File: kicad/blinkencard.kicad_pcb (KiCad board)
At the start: 4 copper layers, 88.9 x 50.8 mm, 64 parts, among them Q1 BC847, Q2 BC847, Q3 BC847, Q4 BC847, Q5 BC847, U1 ICE40UP5K-SG48ITR, U2 ESP32-WROOM-32D

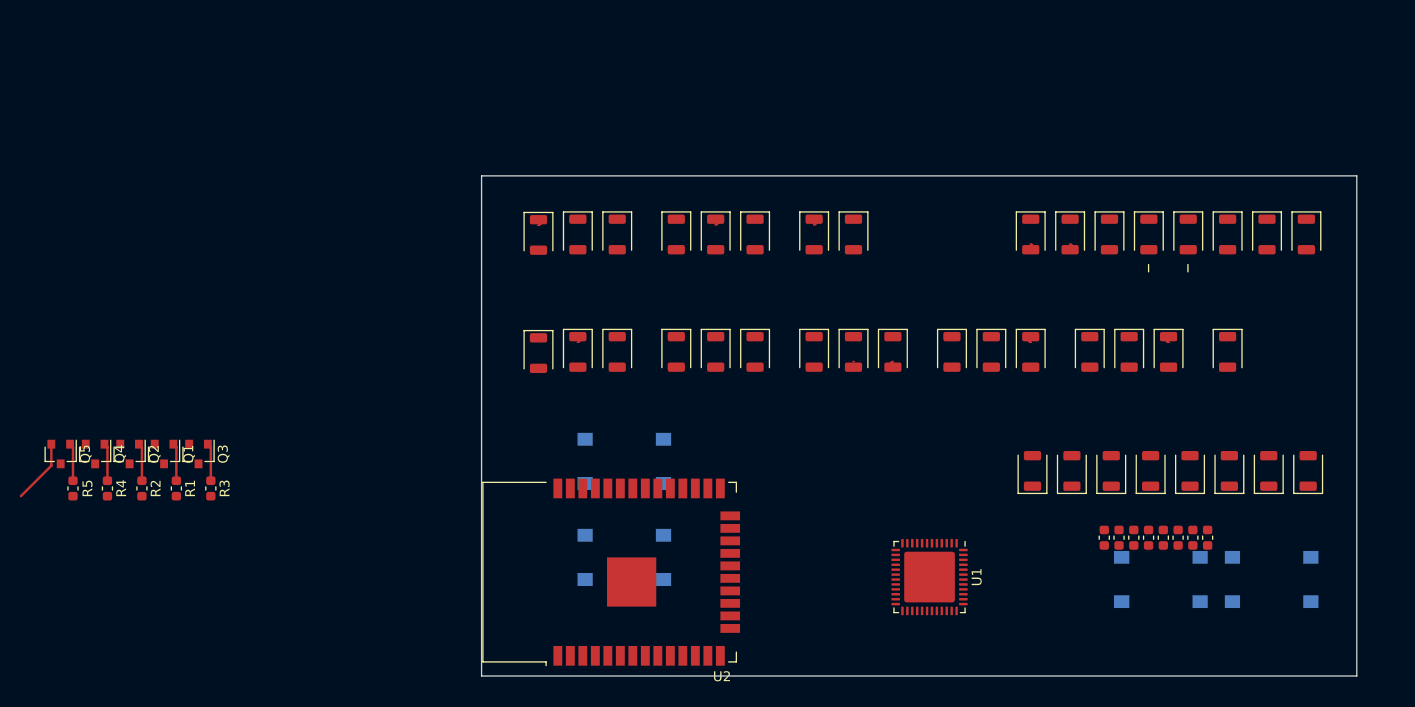
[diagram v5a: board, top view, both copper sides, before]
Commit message: Use CP2102A USB-UART and GPIO instead of ESP32 to keep it simple. Add power section and start routing.
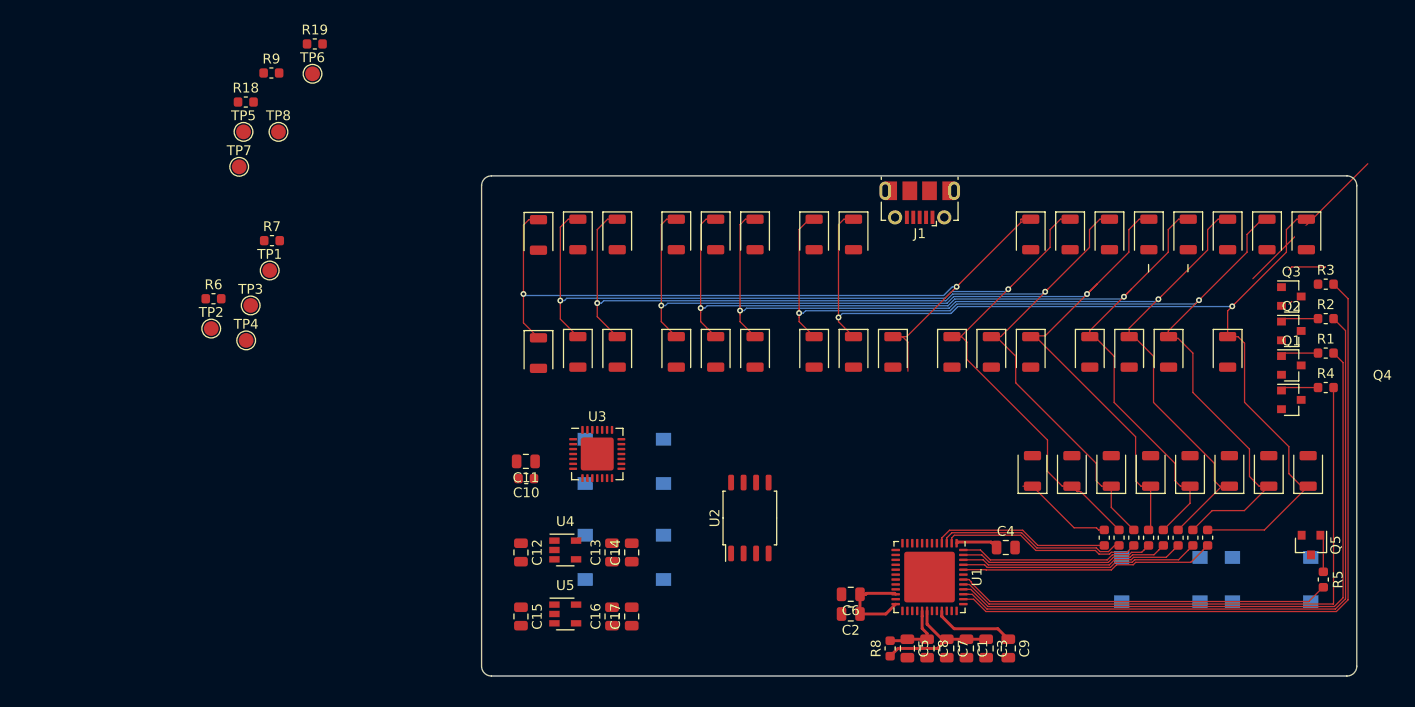
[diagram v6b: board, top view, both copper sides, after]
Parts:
- added C1: 0.01uF, Capacitor_SMD:C_0805_2012Metric, F.Cu at (49.2, 48.0)
- added C10: .1uF, Capacitor_SMD:C_0603_1608Metric, F.Cu at (4.54, 30.8)
- added C11: 4.7uF, Capacitor_SMD:C_0805_2012Metric, F.Cu at (4.50, 29.0)
- added C12: 1.0uF, Capacitor_SMD:C_0805_2012Metric, F.Cu at (4.00, 38.2)
- added C13: 1.0uF, Capacitor_SMD:C_0805_2012Metric, F.Cu at (13.2, 38.2)
- added C14: 10uF, Capacitor_SMD:C_0805_2012Metric, F.Cu at (15.2, 38.2)
- added C15: 1.0uF, Capacitor_SMD:C_0805_2012Metric, F.Cu at (4.00, 44.8)
- added C16: 1.0uF, Capacitor_SMD:C_0805_2012Metric, F.Cu at (13.2, 44.8)
- added C17: 10uF, Capacitor_SMD:C_0805_2012Metric, F.Cu at (15.2, 44.8)
- added C2: 0.01uF, Capacitor_SMD:C_0805_2012Metric, F.Cu at (37.5, 44.5)
- added C3: 0.1uF, Capacitor_SMD:C_0805_2012Metric, F.Cu at (51.2, 48.0)
- added C4: 0.1uF, Capacitor_SMD:C_0805_2012Metric, F.Cu at (53.2, 37.8)
- added C5: 0.01uF, Capacitor_SMD:C_0805_2012Metric, F.Cu at (43.2, 48.0)
- added C6: 0.1uF, Capacitor_SMD:C_0805_2012Metric, F.Cu at (37.5, 42.5)
- added C7: 1uF, Capacitor_SMD:C_0805_2012Metric, F.Cu at (47.2, 48.0)
- added C8: 0.1uF, Capacitor_SMD:C_0805_2012Metric, F.Cu at (45.2, 48.0)
- added C9: 0.1uF, Capacitor_SMD:C_0805_2012Metric, F.Cu at (53.5, 48.0)
- added J1: USB_B_Micro, Connector_USB:USB_Micro-B_Molex-105017-0001, F.Cu at (44.5, 2.75)
- added R18: 47.5K, Resistor_SMD:R_0603_1608Metric, F.Cu at (-23.9, -7.50)
- added R19: 10k, Resistor_SMD:R_0603_1608Metric, F.Cu at (-16.9, -13.4)
- added R6: 10K, Resistor_SMD:R_0603_1608Metric, F.Cu at (-27.2, 12.5)
- added R7: 10K, Resistor_SMD:R_0603_1608Metric, F.Cu at (-21.3, 6.58)
- added R8: 100, Resistor_SMD:R_0603_1608Metric, F.Cu at (41.5, 48.0)
- added R9: 22.1K, Resistor_SMD:R_0603_1608Metric, F.Cu at (-21.4, -10.4)
- added TP1: IOT_49a, TestPoint:TestPoint_Pad_D1.5mm, F.Cu at (-21.5, 9.61)
- added TP2: IOT_48b, TestPoint:TestPoint_Pad_D1.5mm, F.Cu at (-27.5, 15.5)
- added TP3: IOT_46b_G0, TestPoint:TestPoint_Pad_D1.5mm, F.Cu at (-23.4, 13.2)
- added TP4: IOT_45a_G1, TestPoint:TestPoint_Pad_D1.5mm, F.Cu at (-23.9, 16.7)
- added TP5: FPGA_RTS, TestPoint:TestPoint_Pad_D1.5mm, F.Cu at (-24.2, -4.47)
- added TP6: FPGA_CTS, TestPoint:TestPoint_Pad_D1.5mm, F.Cu at (-17.2, -10.4)
- added TP7: FPGA_TXO, TestPoint:TestPoint_Pad_D1.5mm, F.Cu at (-24.6, -0.92)
- added TP8: FPGA_RXI, TestPoint:TestPoint_Pad_D1.5mm, F.Cu at (-20.6, -4.47)
- added U3: CP2102N-A01-GQFN28, Package_DFN_QFN:QFN-28-1EP_5x5mm_P0.5mm_EP3.35x3.35mm, F.Cu at (11.8, 28.2)
- added U4: MIC5504-1.2YM5, Package_TO_SOT_SMD:SOT-23-5, F.Cu at (8.50, 38.0)
- added U5: MIC5504-3.3YM5, Package_TO_SOT_SMD:SOT-23-5, F.Cu at (8.50, 44.5)
- SW1: renamed from REF**; value SW_SPST_PTS645 -> 0
- SW2: renamed from REF**; value SW_SPST_PTS645 -> 1
- SW3: renamed from REF**; value SW_SPST_PTS645 -> LEFT
- SW4: renamed from REF**; value SW_SPST_PTS645 -> RIGHT
- U2: value ESP32-WROOM-32D -> W25Q64JV; footprint RF_Module:ESP32-WROOM-32 -> Package_SO:SOIC-8_5.23x5.23mm_P1.27mm
- moved Q5 127.3 mm to (84.2, 37.5)
- moved R5 127.3 mm to (85.5, 41.0)
- moved R4 124.2 mm to (85.8, 21.5), turned to 0 degrees
- moved Q4 121.6 mm to (82.2, 22.8), turned to 0 degrees
- moved R2 121.5 mm to (85.8, 14.5), turned to 0 degrees
- moved Q2 118.7 mm to (82.2, 15.8), turned to 0 degrees
- moved R1 117.6 mm to (85.8, 18.0), turned to 0 degrees
- moved R3 115.1 mm to (85.8, 11.0), turned to 0 degrees
- moved Q1 114.9 mm to (82.2, 19.2), turned to 0 degrees
- moved Q3 112.1 mm to (82.2, 12.2), turned to 0 degrees
- moved U2 12.5 mm to (27.2, 34.8)
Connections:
- D10 pad 1: Net-(D17-Pad1) -> Net-(D10-Pad1)
- D10 pad 2: Net-(D20-Pad2) -> Net-(D10-Pad2)
- D11 pad 1: Net-(D16-Pad1) -> Net-(D11-Pad1)
- D11 pad 2: Net-(D20-Pad2) -> Net-(D10-Pad2)
- D12 pad 1: Net-(D15-Pad1) -> Net-(D12-Pad1)
- D12 pad 2: Net-(D20-Pad2) -> Net-(D10-Pad2)
- D13 pad 1: Net-(D14-Pad1) -> Net-(D13-Pad1)
- D13 pad 2: Net-(D20-Pad2) -> Net-(D10-Pad2)
- D14 pad 1: Net-(D13-Pad1) -> Net-(D14-Pad1)
- D14 pad 2: Net-(D20-Pad2) -> Net-(D10-Pad2)
- D15 pad 1: Net-(D12-Pad1) -> Net-(D15-Pad1)
- D15 pad 2: Net-(D20-Pad2) -> Net-(D10-Pad2)
- D16 pad 1: Net-(D11-Pad1) -> Net-(D16-Pad1)
- D16 pad 2: Net-(D20-Pad2) -> Net-(D10-Pad2)
- D17 pad 1: Net-(D10-Pad1) -> Net-(D17-Pad1)
- D17 pad 2: Net-(D20-Pad2) -> Net-(D10-Pad2)
- D20 pad 2: Net-(D10-Pad2) -> Net-(D20-Pad2)
- D21 pad 2: Net-(D10-Pad2) -> Net-(D20-Pad2)
- D22 pad 2: Net-(D10-Pad2) -> Net-(D20-Pad2)
- D23 pad 2: Net-(D10-Pad2) -> Net-(D20-Pad2)
- D24 pad 2: Net-(D10-Pad2) -> Net-(D20-Pad2)
- D25 pad 2: Net-(D10-Pad2) -> Net-(D20-Pad2)
- D26 pad 2: Net-(D10-Pad2) -> Net-(D20-Pad2)
- D27 pad 2: Net-(D10-Pad2) -> Net-(D20-Pad2)
- D30 pad 1: Net-(D17-Pad1) -> Net-(D10-Pad1)
- D30 pad 2: Net-(D40-Pad2) -> Net-(D30-Pad2)
- D31 pad 1: Net-(D16-Pad1) -> Net-(D11-Pad1)
- D31 pad 2: Net-(D40-Pad2) -> Net-(D30-Pad2)
- D32 pad 1: Net-(D15-Pad1) -> Net-(D12-Pad1)
- D32 pad 2: Net-(D40-Pad2) -> Net-(D30-Pad2)
- D33 pad 1: Net-(D14-Pad1) -> Net-(D13-Pad1)
- D33 pad 2: Net-(D40-Pad2) -> Net-(D30-Pad2)
- D34 pad 1: Net-(D13-Pad1) -> Net-(D14-Pad1)
- D34 pad 2: Net-(D40-Pad2) -> Net-(D30-Pad2)
- D35 pad 1: Net-(D12-Pad1) -> Net-(D15-Pad1)
- D35 pad 2: Net-(D40-Pad2) -> Net-(D30-Pad2)
- D36 pad 1: Net-(D11-Pad1) -> Net-(D16-Pad1)
- D36 pad 2: Net-(D40-Pad2) -> Net-(D30-Pad2)
- D37 pad 1: Net-(D10-Pad1) -> Net-(D17-Pad1)
- D37 pad 2: Net-(D40-Pad2) -> Net-(D30-Pad2)
- D40 pad 2: Net-(D30-Pad2) -> Net-(D40-Pad2)
- D41 pad 2: Net-(D30-Pad2) -> Net-(D40-Pad2)
- D42 pad 2: Net-(D30-Pad2) -> Net-(D40-Pad2)
- D43 pad 2: Net-(D30-Pad2) -> Net-(D40-Pad2)
- D44 pad 2: Net-(D30-Pad2) -> Net-(D40-Pad2)
- D45 pad 2: Net-(D30-Pad2) -> Net-(D40-Pad2)
- D46 pad 2: Net-(D30-Pad2) -> Net-(D40-Pad2)
- D47 pad 2: Net-(D30-Pad2) -> Net-(D40-Pad2)
- D50 pad 1: Net-(D17-Pad1) -> Net-(D10-Pad1)
- D51 pad 1: Net-(D16-Pad1) -> Net-(D11-Pad1)
- D52 pad 1: Net-(D15-Pad1) -> Net-(D12-Pad1)
- D53 pad 1: Net-(D14-Pad1) -> Net-(D13-Pad1)
- D54 pad 1: Net-(D13-Pad1) -> Net-(D14-Pad1)
- D55 pad 1: Net-(D12-Pad1) -> Net-(D15-Pad1)
- D56 pad 1: Net-(D11-Pad1) -> Net-(D16-Pad1)
- D57 pad 1: Net-(D10-Pad1) -> Net-(D17-Pad1)
- SW1 pad 1: (no net) -> BUTTON_0
- SW1 pad 2: (no net) -> GND
- SW2 pad 1: (no net) -> BUTTON_1
- SW2 pad 2: (no net) -> GND
- SW3 pad 1: (no net) -> BUTTON_L
- SW3 pad 2: (no net) -> GND
- SW4 pad 1: (no net) -> BUTTON_R
- SW4 pad 2: (no net) -> GND
- U1 pad 10: LED_ROW_2 -> Net-(U1-Pad10)
- U1 pad 11: LED_ROW_1 -> FPGA_RTS
- U1 pad 12: LED_ROW_0 -> FPGA_CTS
- U1 pad 14: Net-(U1-Pad14) -> FPGA_SO_FLASH_MOSI
- U1 pad 15: Net-(U1-Pad15) -> FPGA_SCK
- U1 pad 16: Net-(U1-Pad16) -> FPGA_SS
- U1 pad 17: Net-(U1-Pad17) -> FPGA_SI_FLASH_MISO
- U1 pad 19: Net-(U1-Pad19) -> FLASH_HOLDn
- U1 pad 23: Net-(U1-Pad23) -> BUTTON_1
- U1 pad 25: Net-(U1-Pad25) -> BUTTON_0
- U1 pad 26: Net-(U1-Pad26) -> BUTTON_R
- U1 pad 27: Net-(U1-Pad27) -> BUTTON_L
- U1 pad 29: +1V2 -> Net-(C5-Pad1)
- U1 pad 38: Net-(U1-Pad38) -> LED_ROW_2
- U1 pad 39: Net-(U1-Pad39) -> LED_ROW_1
- U1 pad 40: Net-(U1-Pad40) -> LED_ROW_0
- U1 pad 41: Net-(U1-Pad41) -> LED_ROW_3
- U1 pad 42: Net-(U1-Pad42) -> LED_ROW_4
- U1 pad 6: LED_ROW_4 -> Net-(U1-Pad6)
- U1 pad 7: Net-(U1-Pad7) -> FPGA_CDONE
- U1 pad 8: Net-(U1-Pad8) -> FPGA_CRESET
- U1 pad 9: LED_ROW_3 -> Net-(U1-Pad9)
- U2 pad 1: Net-(U2-Pad1) -> FPGA_SS
- U2 pad 2: Net-(U2-Pad2) -> FPGA_SI_FLASH_MISO
- U2 pad 3: Net-(U2-Pad3) -> VDD
- U2 pad 4: Net-(U2-Pad4) -> GND
- U2 pad 5: Net-(U2-Pad5) -> FPGA_SO_FLASH_MOSI
- U2 pad 6: Net-(U2-Pad6) -> FPGA_SCK
- U2 pad 7: Net-(U2-Pad7) -> FLASH_HOLDn
- U2 pad 8: Net-(U2-Pad8) -> VDD
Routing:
- net Net-(D10-Pad1): track 0.00 -> 108.7 mm, vias 0 -> 2
- net Net-(D12-Pad1): track 0.00 -> 104.7 mm, vias 0 -> 2
- net Net-(D11-Pad1): track 1.57 -> 106.0 mm, vias 0 -> 2
- net Net-(D14-Pad1): track 0.00 -> 101.2 mm, vias 0 -> 2
- net Net-(D15-Pad1): track 0.00 -> 100.7 mm, vias 0 -> 2
- net Net-(D17-Pad1): track 1.57 -> 101.7 mm, vias 0 -> 2
- net Net-(D13-Pad1): track 3.15 -> 102.8 mm, vias 0 -> 2
- net Net-(D16-Pad1): track 2.59 -> 101.3 mm, vias 0 -> 2
- net LED_ROW_2: track 0.00 -> 72.8 mm
- net LED_ROW_1: track 0.00 -> 68.8 mm
- net LED_ROW_0: track 0.00 -> 64.9 mm
- net LED_ROW_3: track 0.00 -> 60.4 mm
- net LED_ROW_4: track 0.00 -> 38.2 mm
- net LED_COL_7: track 0.00 -> 25.9 mm
- net LED_COL_6: track 0.00 -> 24.3 mm
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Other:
- outline, holes or cut-outs redrawn
- copper layers 4 -> 2
- net class Default: clearance 0.2 -> 0.127; trace_width 0.25 -> 0.127; via_dia 0.8 -> 0.6; via_drill 0.4 -> 0.3
- rule pad_to_mask_clearance: 0.051 -> 0.2
- rule trace_clearance: 0.2 -> 0.127
- rule trace_min: 0.2 -> 0.127
- rule via_min_size: 0.4 -> 0.6

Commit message: LED routing
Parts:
- removed the Q4 at (82.2, 22.8)
- added Q1: BC847, Package_TO_SOT_SMD:SOT-23, F.Cu at (82.2, 22.8)
- turned D50 to 270 degrees
- turned D51 to 270 degrees
- turned D52 to 270 degrees
- turned D53 to 270 degrees
- turned D54 to 270 degrees
- turned D55 to 270 degrees
- turned D56 to 270 degrees
- turned D57 to 270 degrees
- renumbered Q1 to Q2, Q2 to Q3, Q3 to Q4, R4 to R1, R1 to R2, R2 to R3, R3 to R4
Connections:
- Q2 pad 2: Net-(D10-Pad2) -> Net-(D20-Pad2)
- Q3 pad 2: Net-(D20-Pad2) -> Net-(D30-Pad2)
- Q4 pad 2: Net-(D30-Pad2) -> Net-(D40-Pad2)
- R1 pad 2: LED_ROW_3 -> LED_ROW_0
- R2 pad 2: LED_ROW_0 -> LED_ROW_1
- R3 pad 2: LED_ROW_1 -> LED_ROW_2
- R4 pad 2: LED_ROW_2 -> LED_ROW_3
- U1 pad 38: LED_ROW_2 -> LED_ROW_3
- U1 pad 39: LED_ROW_1 -> LED_ROW_2
- U1 pad 40: LED_ROW_0 -> LED_ROW_1
- U1 pad 41: LED_ROW_3 -> LED_ROW_0
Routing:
- net Net-(D30-Pad2): track 0.00 -> 92.4 mm, vias 0 -> 9
- net Net-(D10-Pad2): track 0.00 -> 78.3 mm, vias 0 -> 2
- net Net-(D40-Pad2): track 0.00 -> 45.9 mm, vias 0 -> 9
- net Net-(D20-Pad2): track 0.00 -> 43.1 mm, vias 0 -> 9
- net Net-(D50-Pad2): track 0.00 -> 40.0 mm, vias 0 -> 8
- net Net-(D10-Pad1): track 108.7 -> 91.9 mm
- net VDD: track 22.4 -> 38.4 mm, vias 0 -> 4
- net Net-(D12-Pad1): track 104.7 -> 91.8 mm
- net LED_ROW_3: track 60.4 -> 72.8 mm
- net Net-(D11-Pad1): track 106.0 -> 93.7 mm
- net Net-(D13-Pad1): track 102.8 -> 91.5 mm
- net Net-(D14-Pad1): track 101.2 -> 93.7 mm
- net Net-(D16-Pad1): track 101.3 -> 94.2 mm
- net Net-(D15-Pad1): track 100.7 -> 94.1 mm
- net Net-(D17-Pad1): track 101.7 -> 96.7 mm
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
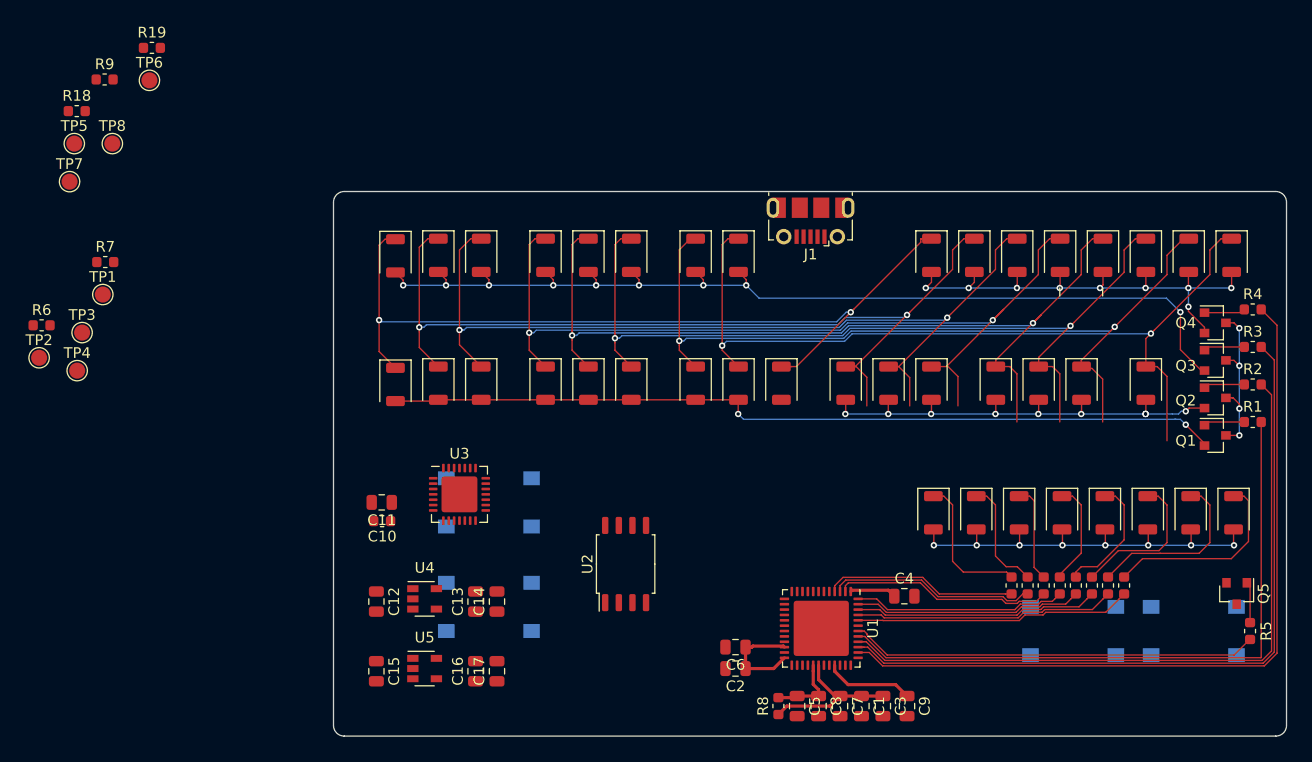
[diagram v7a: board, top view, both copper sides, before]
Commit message: Mostly routed
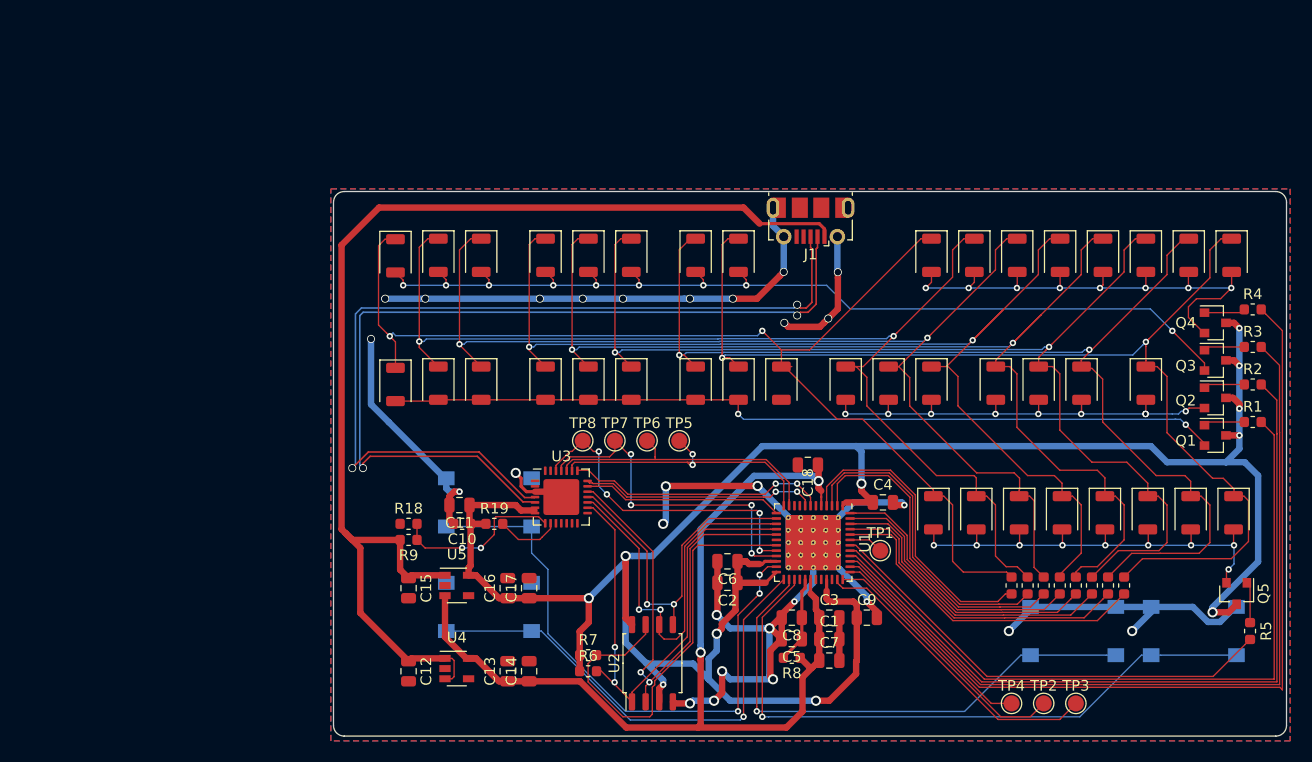
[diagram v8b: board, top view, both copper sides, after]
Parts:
- added C18: 0.1uF, Capacitor_SMD:C_0805_2012Metric, F.Cu at (44.2, 25.5)
- D10, D11, D12, D13, D14, D15, D16, D17, D20, D21, D22, D23, D24, D25, D26, D27, D30, D31, D32, D33, D34, D35, D36, D37, D40, D41, D42, D43, D44, D45, D46, D47, D50, D51, D52, D53, D54, D55, D56, D57: footprint LED_SMD:LED_1206_3216Metric_ReverseMount_Hole1.8x2.4mm -> blinkencard:LED_1206_3216Metric_ReverseMount_Hole1.8x2.4mm
- J1: footprint Connector_USB:USB_Micro-B_Molex-105017-0001 -> blinkencard:USB_Micro-B_Molex-105017-0001
- U1: footprint Package_DFN_QFN:QFN-48-1EP_7x7mm_P0.5mm_EP5.15x5.15mm -> Package_DFN_QFN:QFN-48-1EP_7x7mm_P0.5mm_EP5.15x5.15mm_ThermalVias
- U2: footprint Package_SO:SOIC-8_5.23x5.23mm_P1.27mm -> Package_SO:SOIC-8_5.275x5.275mm_P1.27mm
- moved TP2 99.1 mm to (66.2, 47.8)
- moved TP3 98.9 mm to (69.2, 47.8)
- moved TP4 92.5 mm to (63.2, 47.8)
- moved TP1 76.4 mm to (51.0, 33.5)
- moved TP5 62.9 mm to (32.2, 23.2)
- moved R6 60.3 mm to (23.8, 44.8)
- moved R7 58.1 mm to (23.8, 43.2)
- moved TP6 57.3 mm to (29.2, 23.2)
- moved TP7 56.3 mm to (26.2, 23.2)
- moved R19 54.7 mm to (15.0, 31.0)
- moved TP8 51.9 mm to (23.2, 23.2)
- moved R9 51.5 mm to (7.00, 32.5), turned to 180 degrees
- moved R18 49.4 mm to (7.00, 31.0)
- moved C3 9.65 mm to (46.2, 39.8), turned to 0 degrees
- moved U2 9.58 mm to (29.8, 44.0)
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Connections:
- net Net-(J1-Pad2) renamed /usb_and_power/D-
- net Net-(J1-Pad3) renamed /usb_and_power/D+
- U1 pad 11: FPGA_RTS -> FPGA_CTS
- U1 pad 12: FPGA_CTS -> FPGA_RTS
- U3 pad 21: FPGA_CDONE -> FPGA_CRESET
- U3 pad 22: FPGA_CRESET -> FPGA_CDONE
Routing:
- net GND: track 0.00 -> 194.7 mm, vias 0 -> 28
- net VDD: track 38.4 -> 223.4 mm, vias 4 -> 11
- net +5V: track 0.00 -> 109.1 mm
- net /usb_and_power/D+: track 0.00 -> 83.4 mm, vias 0 -> 2
- net /usb_and_power/D-: track 0.00 -> 82.5 mm, vias 0 -> 2
- net +1V2: track 14.4 -> 91.9 mm, vias 0 -> 2
- net BUTTON_L: track 0.00 -> 60.7 mm, vias 0 -> 1
- net BUTTON_1: track 0.00 -> 54.8 mm, vias 0 -> 3
- net BUTTON_R: track 0.00 -> 49.2 mm, vias 0 -> 1
- net FPGA_SS: track 0.00 -> 47.9 mm, vias 0 -> 2
- net FPGA_SI_FLASH_MISO: track 0.00 -> 46.0 mm, vias 0 -> 2
- net BUTTON_0: track 0.00 -> 45.7 mm, vias 0 -> 1
- net FLASH_HOLDn: track 0.00 -> 41.8 mm
- net FPGA_SCK: track 0.00 -> 36.8 mm, vias 0 -> 2
- net FPGA_SO_FLASH_MOSI: track 0.00 -> 32.7 mm, vias 0 -> 2
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- added copper zone on B.Cu, net GND
- added copper zone on F.Cu, net GND
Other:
- net class PWR added: clearance 0.127, trace_width 0.6, via_dia 0.95, via_drill 0.6
